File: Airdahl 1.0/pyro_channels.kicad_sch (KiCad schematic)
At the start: 17 parts, among them J5 TBL002A-350-08GY-2GY, Q1 2N7002, Q2 2N7002, Q3 2N7002, Q4 2N7002

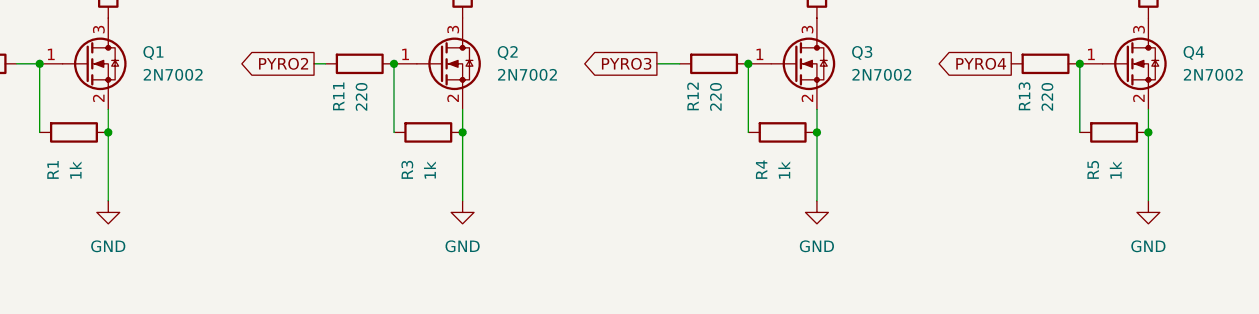
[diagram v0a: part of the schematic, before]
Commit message: added 5v buck, h bridge IC, updated jtag connections
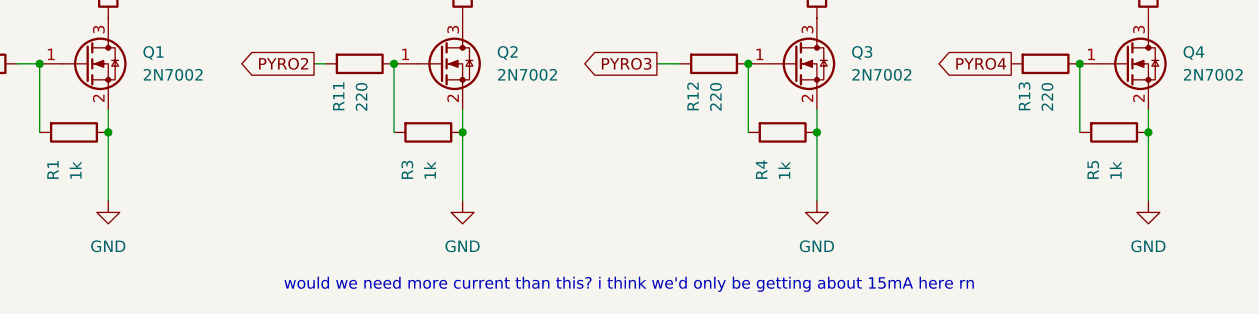
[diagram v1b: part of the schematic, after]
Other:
- note added: "would we need more current than this? i think we'd only be getting about 15mA here rn"

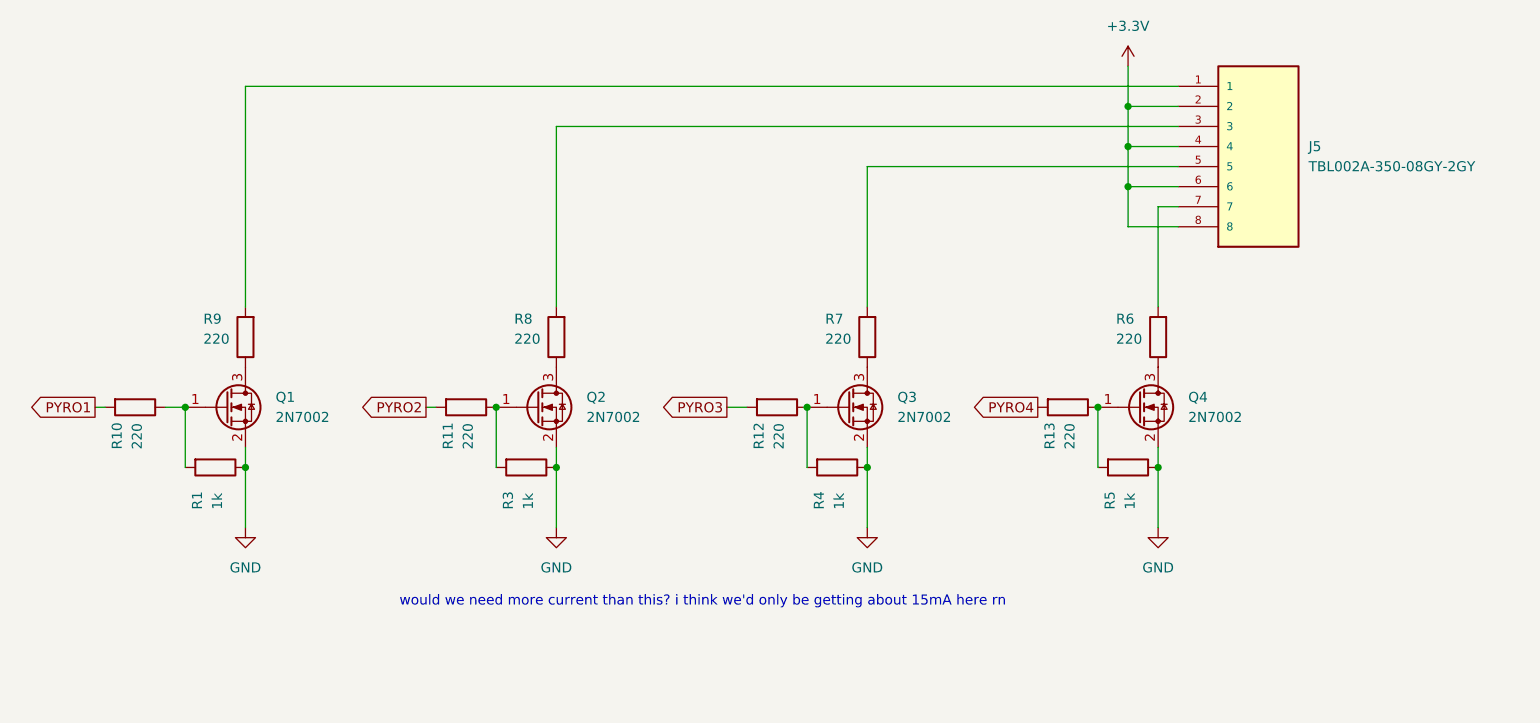
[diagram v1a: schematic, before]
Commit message: reworked pyro circuit for higher current, split off pyro 3.3v into its own rail, some schematic cleanup
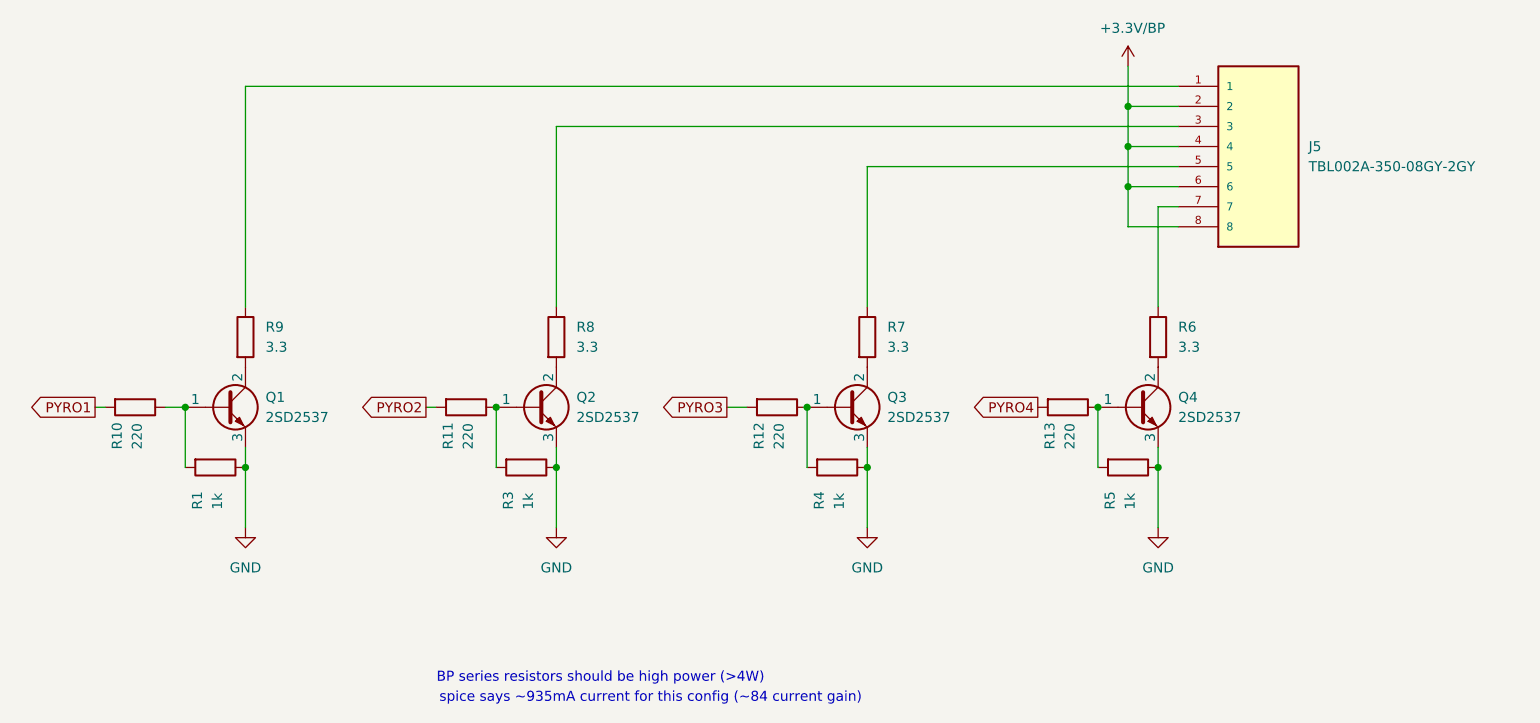
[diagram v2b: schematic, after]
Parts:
- removed Q1, Q2, Q3, Q4: 2N7002, Package_TO_SOT_SMD:SOT-23, symbol Transistor_FET:2N7002
- added Q1, Q2, Q3, Q4: 2SD2537, Package_TO_SOT_SMD:SOT-89-3, symbol Simulation_SPICE:NPN
- R6, R7, R8, R9: value 220 -> 3.3; footprint Resistor_SMD:R_0603_1608Metric -> Resistor_SMD:R_2512_6332Metric
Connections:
- net GND: now also Q1.3, Q2.3, Q3.3, Q4.3
- net at R8.1: now also J5.3
- net at R8.2: now also Q2.2; no longer J5.3
- net at R13.1, R5.2: now also Q4.1
- net at R6.1: now also J5.7
- net at R12.1, R4.2: now also Q3.1
- net at R11.1, R3.2: now also Q2.1
- net at R7.1: now also J5.5
- net at R9.1: now also J5.1
- net at R9.2: now also Q1.2; no longer J5.1
- net at R1.2, R10.1: now also Q1.1
- net at R7.2: now also Q3.2; no longer J5.5
- net at R6.2: now also Q4.2; no longer J5.7
- net +3.3V renamed +3.3V/BP
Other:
- note added: "BP series resistors should be high power (>4W)"
- note added: "spice says ~935mA current for this config (~84 current gain)"
- note removed: "would we need more current than this? i think we'd only be getting about 15mA here rn"
